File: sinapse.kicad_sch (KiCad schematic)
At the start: 34 parts

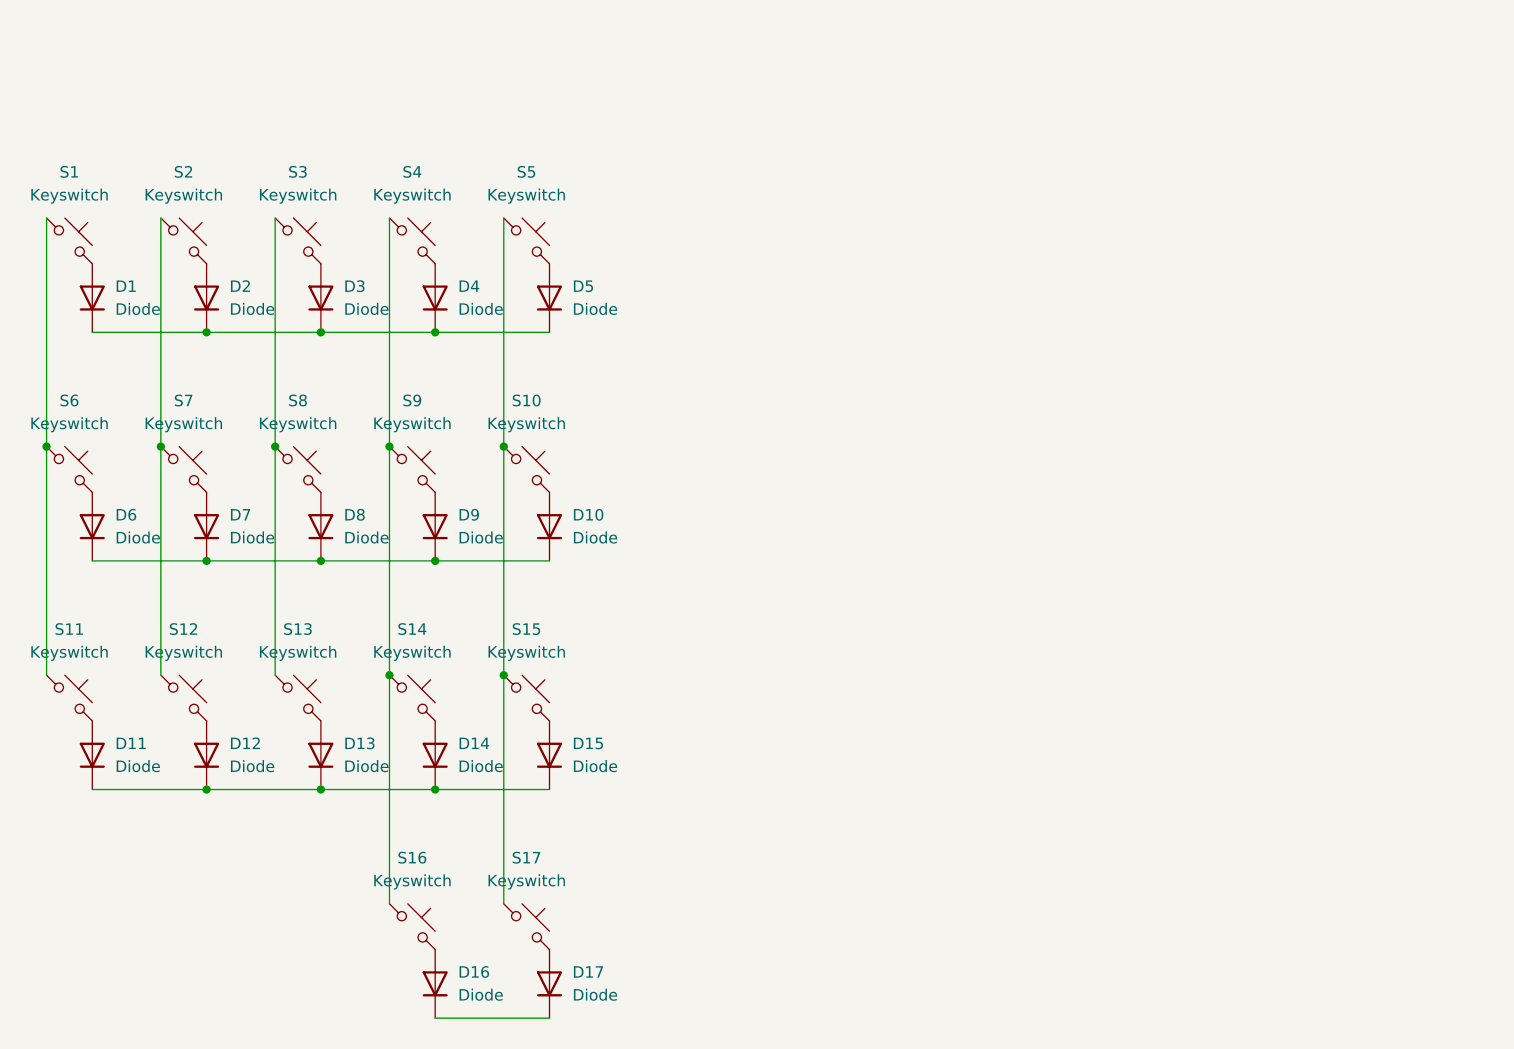
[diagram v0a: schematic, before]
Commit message: connected rows and cols to pro micro with global labels
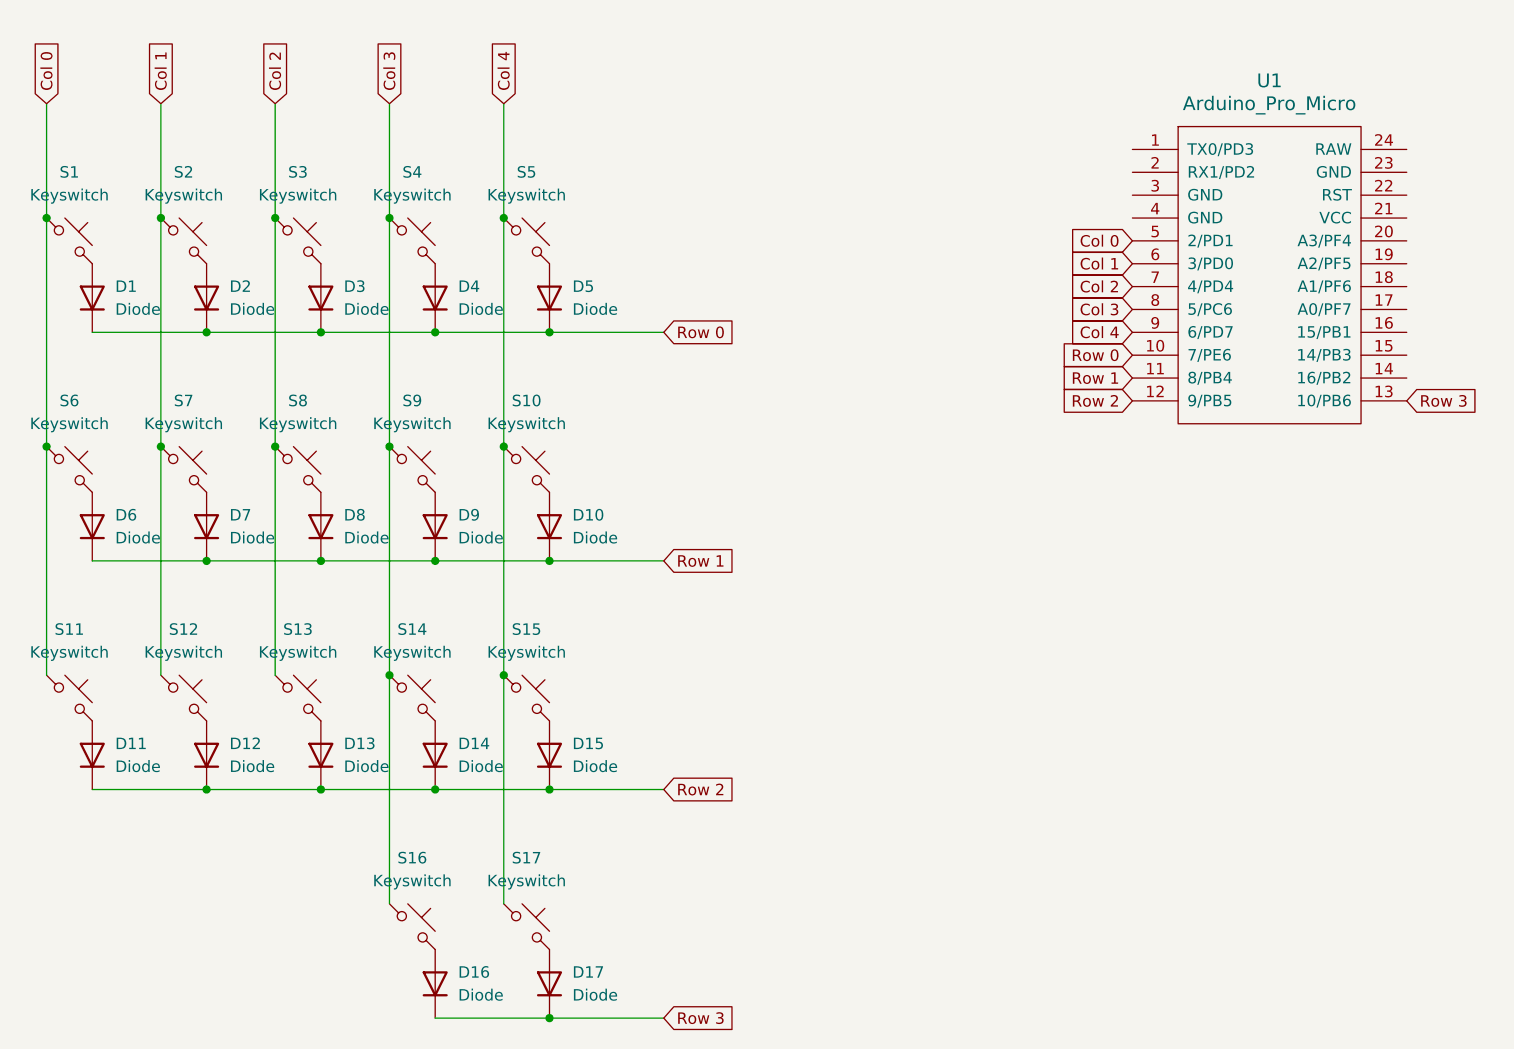
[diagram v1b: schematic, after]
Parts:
- added U1: Arduino_Pro_Micro, ScottoKeebs_MCU:Arduino_Pro_Micro, symbol ScottoKeebs:MCU_Arduino_Pro_Micro
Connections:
- net Row 1: now reaches D10.1 (K), D6.1 (K), D7.1 (K), D8.1 (K), D9.1 (K)
- net Row 1: now also U1.11 (8/PB4)
- net Col 3: now reaches S14.1, S16.1, S4.1, S9.1
- net Col 3: now also U1.8 (5/PC6)
- net Col 4: now reaches S10.1, S15.1, S17.1, S5.1
- net Col 4: now also U1.9 (6/PD7)
- net Col 1: now reaches S12.1, S2.1, S7.1
- net Col 1: now also U1.6 (3/PD0)
- net Row 0: now reaches D1.1 (K), D2.1 (K), D3.1 (K), D4.1 (K), D5.1 (K)
- net Row 0: now also U1.10 (7/PE6)
- net Row 2: now reaches D11.1 (K), D12.1 (K), D13.1 (K), D14.1 (K), D15.1 (K)
- net Row 2: now also U1.12 (9/PB5)
- net Col 2: now reaches S13.1, S3.1, S8.1
- net Col 2: now also U1.7 (4/PD4)
- net Col 0: now reaches S1.1, S11.1, S6.1
- net Col 0: now also U1.5 (2/PD1)
- net Row 3: now reaches D16.1 (K), D17.1 (K)
- net Row 3: now also U1.13 (10/PB6)
